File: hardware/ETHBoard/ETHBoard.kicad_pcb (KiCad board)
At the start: 2 copper layers, 25.1 x 12.2 mm, 24 parts, among them J1 Conn_02x04_Odd_Even, J2 Conn_01x02_Pin, U1 LAN8651B1-E_LMX, Y1 X322525MOB4SI

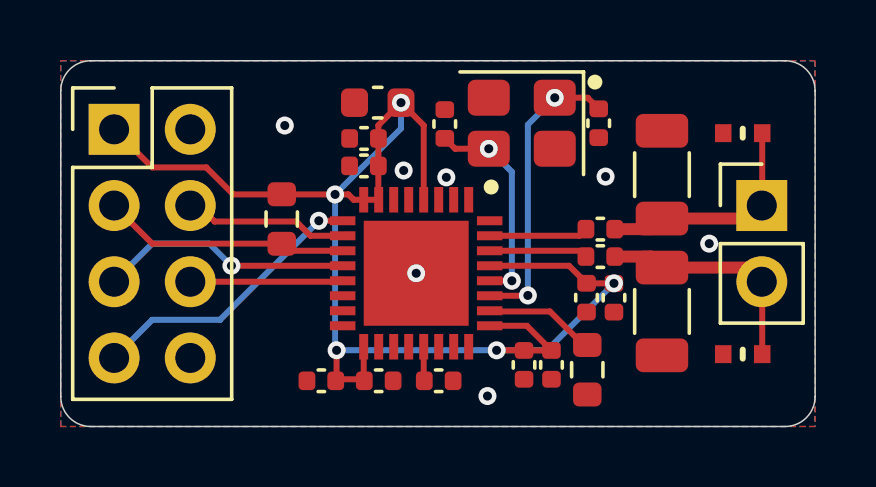
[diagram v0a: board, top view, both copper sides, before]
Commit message: Fixed vias in small pads.
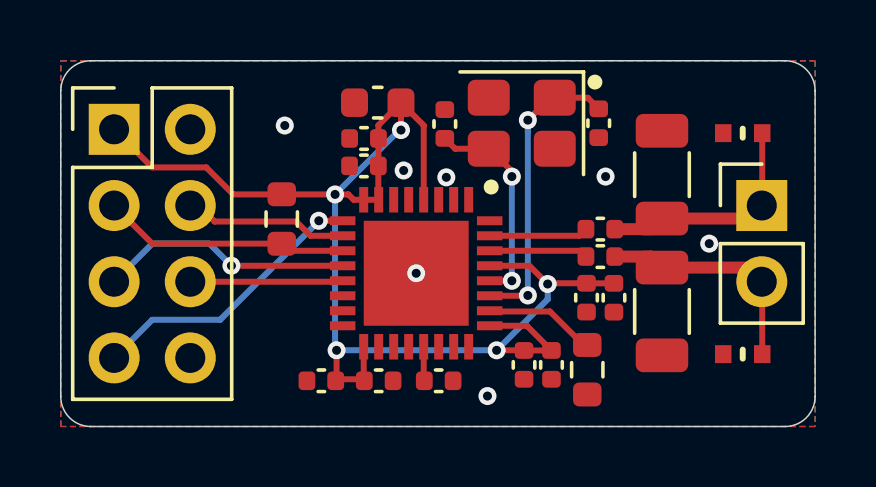
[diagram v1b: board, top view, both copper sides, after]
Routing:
- net 3V3: track 47.8 -> 46.0 mm
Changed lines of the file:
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@@
 		(sheetname "/")
 		(sheetfile "ETHBoard.kicad_sch")
+		(clearance 0.15)
 		(attr smd)
 		(fp_circle
@@
 			(layer "F.Fab")
 		)
-		(fp_text user "${REFERENCE}"
-			(at 0 0 90)
-			(layer "F.Fab")
-			(effects
-				(font
-					(size 1.27 1.27)
-					(thickness 0.254)
-				)
-			)
-		)
 		(pad "1" smd rect
 			(at -2.45 -1.75)
@@
 	)
 	(via
-		(at 85.508 57.884)
+		(at 85.09 54.4576)
 		(size 0.6)
 		(drill 0.3)
 		(layers "F.Cu" "B.Cu")
+		(free yes)
 		(net 2)
 	)
 	(via
-		(at 85.09 54.4576)
+		(at 85.508 57.884)
 		(size 0.6)
 		(drill 0.3)
 		(layers "F.Cu" "B.Cu")
-		(free yes)
 		(net 2)
 	)
@@
 	)
 	(segment
+		(start 89.229843 52.779562)
+		(end 89.976605 52.0328)
+		(width 0.2)
+		(layer "F.Cu")
+		(net 3)
+	)
+	(segment
 		(start 89.2194 58.634)
 		(end 89.2302 58.6232)
@@
 	)
 	(segment
+		(start 89.976605 52.0328)
+		(end 90.127 52.0328)
+		(width 0.2)
+		(layer "F.Cu")
+		(net 3)
+	)
+	(segment
 		(start 87.958 58.634)
 		(end 89.2194 58.634)
@@
 	)
 	(via
-		(at 90.127 52.0328)
+		(at 89.229843 52.779562)
 		(size 0.6)
 		(drill 0.3)
@@
 	)
 	(segment
-		(start 89.2302 52.9296)
-		(end 90.127 52.0328)
+		(start 89.229843 53.16557)
+		(end 89.2302 53.165927)
 		(width 0.2)
 		(layer "B.Cu")
@@
 	)
 	(segment
-		(start 89.2302 58.6232)
-		(end 89.2302 52.9296)
+		(start 89.229843 52.779562)
+		(end 89.229843 53.16557)
 		(width 0.2)
 		(layer "B.Cu")
@@
 	)
 	(segment
+		(start 89.2302 53.165927)
+		(end 89.2302 58.6232)
+		(width 0.2)
+		(layer "B.Cu")
+		(net 3)
+	)
+	(segment
+		(start 87.9466 53.7328)
+		(end 87.927 53.7328)
+		(width 0.2)
+		(layer "F.Cu")
+		(net 4)
+	)
+	(segment
+		(start 88.6968 54.483)
+		(end 87.9466 53.7328)
+		(width 0.2)
+		(layer "F.Cu")
+		(net 4)
+	)
+	(segment
 		(start 86.8062 53.7328)
 		(end 86.4616 53.3882)
@@
 	)
 	(segment
+		(start 88.6968 54.6608)
+		(end 88.6968 54.483)
+		(width 0.2)
+		(layer "F.Cu")
+		(net 4)
+	)
+	(segment
 		(start 88.69669 58.134)
 		(end 87.958 58.134)
@@
 	)
 	(via
-		(at 87.927 53.7328)
+		(at 88.69669 58.134)
 		(size 0.6)
 		(drill 0.3)
@@
 	)
 	(via
-		(at 88.69669 58.134)
+		(at 88.6968 54.6608)
 		(size 0.6)
 		(drill 0.3)
@@
 	)
 	(segment
-		(start 87.927 53.7328)
-		(end 88.69669 54.50249)
+		(start 88.6968 58.13389)
+		(end 88.69669 58.134)
 		(width 0.2)
 		(layer "B.Cu")
@@
 	)
 	(segment
-		(start 88.69669 54.50249)
-		(end 88.69669 58.134)
+		(start 88.6968 54.6608)
+		(end 88.6968 58.13389)
 		(width 0.2)
 		(layer "B.Cu")
@@
 	)
 	(segment
-		(start 91.186 58.2168)
-		(end 90.6032 57.634)
-		(width 0.2)
-		(layer "F.Cu")
-		(net 5)
-	)
-	(segment
 		(start 75.438 53.086)
 		(end 76.708 54.356)
@@
 	)
 	(segment
-		(start 90.6032 57.634)
-		(end 87.958 57.634)
+		(start 85.0014 53.1114)
+		(end 85.0014 52.197)
 		(width 0.2)
 		(layer "F.Cu")
@@
 	)
 	(segment
+		(start 89.8906 58.2422)
+		(end 89.916 58.2168)
+		(width 0.2)
+		(layer "F.Cu")
+		(net 5)
+	)
+	(segment
 		(start 88.1888 60.452)
 		(end 89.098 60.452)
@@
 	)
 	(segment
+		(start 89.2824 57.634)
+		(end 87.958 57.634)
+		(width 0.2)
+		(layer "F.Cu")
+		(net 5)
+	)
+	(segment
 		(start 87.958 59.634)
 		(end 89.1944 59.634)
@@
 	)
 	(segment
+		(start 89.916 58.2168)
+		(end 91.186 58.2168)
+		(width 0.2)
+		(layer "F.Cu")
+		(net 5)
+	)
+	(segment
 		(start 83.2468 55.256)
 		(end 83.4248 55.434)
@@
 	)
 	(segment
+		(start 89.8906 58.2422)
+		(end 89.2824 57.634)
+		(width 0.2)
+		(layer "F.Cu")
+		(net 5)
+	)
+	(segment
 		(start 83.758 55.434)
 		(end 84.258 55.434)
@@
 	)
 	(via
-		(at 82.8548 60.452)
+		(at 89.8906 58.2422)
 		(size 0.6)
 		(drill 0.3)
@@
 	)
 	(via
-		(at 92.1004 58.2194)
+		(at 85.0014 53.1114)
 		(size 0.6)
 		(drill 0.3)
@@
 	)
 	(via
-		(at 85.0014 52.197)
+		(at 82.8548 60.452)
 		(size 0.6)
 		(drill 0.3)
@@
 	)
 	(segment
-		(start 85.0014 53.0586)
-		(end 85.0014 52.197)
+		(start 89.8906 58.2422)
+		(end 89.8906 58.7502)
 		(width 0.2)
 		(layer "B.Cu")
@@
 	)
 	(segment
-		(start 82.8548 60.452)
-		(end 88.1888 60.452)
+		(start 84.9486 53.1114)
+		(end 82.804 55.256)
 		(width 0.2)
 		(layer "B.Cu")
@@
 	)
 	(segment
-		(start 82.804 60.4012)
-		(end 82.804 55.256)
+		(start 82.8548 60.452)
+		(end 88.1888 60.452)
 		(width 0.2)
 		(layer "B.Cu")
@@
 	)
 	(segment
-		(start 82.804 55.256)
-		(end 85.0014 53.0586)
+		(start 89.8906 58.7502)
+		(end 88.1888 60.452)
 		(width 0.2)
 		(layer "B.Cu")
@@
 	)
 	(segment
-		(start 82.8548 60.452)
-		(end 82.804 60.4012)
+		(start 82.804 60.4012)
+		(end 82.804 55.256)
 		(width 0.2)
 		(layer "B.Cu")
@@
 	)
 	(segment
-		(start 89.8678 60.452)
-		(end 92.1004 58.2194)
+		(start 82.8548 60.452)
+		(end 82.804 60.4012)
 		(width 0.2)
 		(layer "B.Cu")
@@
 	)
 	(segment
-		(start 88.1888 60.452)
-		(end 89.8678 60.452)
+		(start 85.0014 53.1114)
+		(end 84.9486 53.1114)
 		(width 0.2)
 		(layer "B.Cu")

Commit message: Rework ETHBoard.
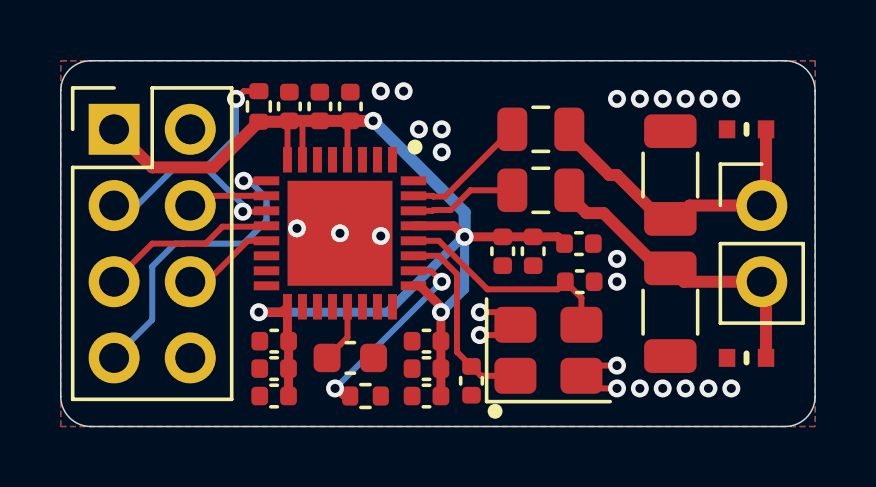
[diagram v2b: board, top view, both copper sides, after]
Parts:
- added C12: 10uF, Capacitor_SMD:C_0402_1005Metric, F.Cu at (80.8, 62.0)
- added C15: 10uF, Capacitor_SMD:C_0402_1005Metric, F.Cu at (85.9, 62.0)
- added C6: 10uF, Capacitor_SMD:C_0402_1005Metric, F.Cu at (90.9, 56.9)
- C1: footprint Capacitor_SMD:C_0402_1005Metric -> Capacitor_SMD:C_0603_1608Metric
- C16: renamed from C13; footprint Capacitor_SMD:C_0402_1005Metric -> Capacitor_SMD:C_0805_2012Metric
- C17: renamed from C14; footprint Capacitor_SMD:C_0402_1005Metric -> Capacitor_SMD:C_0805_2012Metric
- C9: renamed from C4; footprint Capacitor_SMD:C_0603_1608Metric -> Capacitor_SMD:C_0402_1005Metric
- R1, R2: footprint Resistor_SMD:R_0603_1608Metric -> Resistor_SMD:R_0402_1005Metric
- moved C8 12.6 mm to (81.3, 52.3), turned to 90 degrees
- moved C7 10.9 mm to (82.3, 52.3), turned to 90 degrees
- moved C2 9.58 mm to (87.4, 61.5)
- moved Y1 7.62 mm to (89.9, 60.5), turned to 0 degrees
- moved R1 7.45 mm to (83.8, 62.0), turned to 0 degrees
- moved C3 6.92 mm to (91.0, 58.2), turned to 0 degrees
- moved C5 6.78 mm to (89.4, 57.1), turned to -90 degrees
- moved C4 5.43 mm to (88.4, 57.1), turned to -90 degrees
- moved C14 4.17 mm to (85.9, 61.1), turned to 180 degrees
- moved C16 3.87 mm to (89.7, 53.1)
- moved R2 3.83 mm to (80.3, 52.3), turned to -90 degrees
- moved C10 3.73 mm to (80.8, 60.1), turned to 180 degrees
- moved C13 3.35 mm to (85.9, 60.1), turned to 180 degrees
- moved C1 3.04 mm to (83.3, 60.7)
- moved C17 2.97 mm to (89.7, 55.1)
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- renumbered C12 to C10, C10 to C13, C9 to C14, C8 to C4, C7 to C5, C6 to C7, C5 to C8
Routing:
- net GND: track 0.00 -> 5.38 mm, vias 7 -> 25
- net Net-(U1-XTI): track 9.95 -> 6.57 mm, vias 2 -> 0
- net Net-(U1-RBIAS): track 3.73 -> 6.73 mm, vias 0 -> 2
- net /T1S_d-: track 7.65 -> 10.6 mm
- net MISO: track 5.50 -> 2.67 mm
- net SCLK: track 8.45 -> 5.85 mm, vias 1 -> 0
- net /T1S_d+: track 7.67 -> 10.1 mm
- net 3V3: track 46.0 -> 43.6 mm, vias 5 -> 4
- net MOSI: track 5.09 -> 3.10 mm
- net CS_N: track 8.24 -> 9.94 mm, vias 0 -> 2
- net IRQ_N: track 9.52 -> 10.5 mm
- net TRXN: track 3.30 -> 4.23 mm
- net Net-(U1-CCOMP): track 1.08 -> 1.99 mm
- net Net-(U1-XTO): track 7.08 -> 7.50 mm, vias 2 -> 0

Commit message: Added common mode choke.
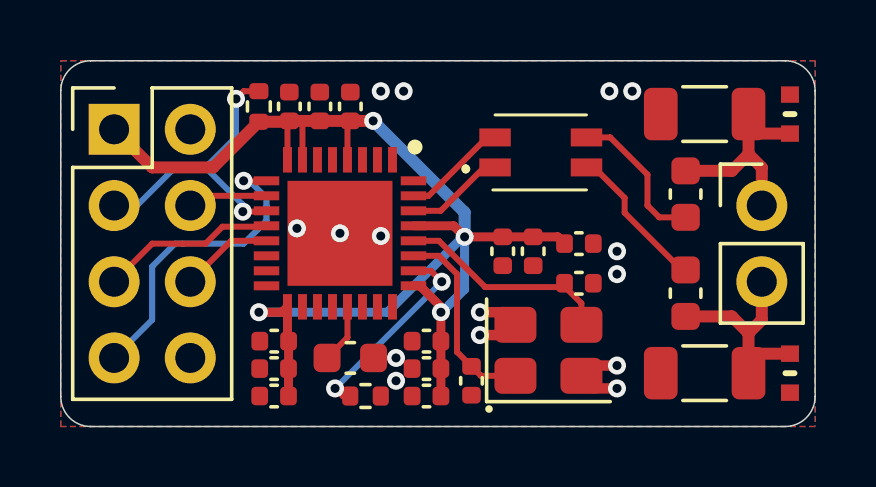
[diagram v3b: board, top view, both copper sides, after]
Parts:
- added FL1: DLW32MH201XK2L, LIB_DLW32MH201XK2L:DLW32MH101XK2L, F.Cu at (89.7, 53.9)
- C16, C17: footprint Capacitor_SMD:C_0805_2012Metric -> Capacitor_SMD:C_0603_1608Metric
- moved C17 5.92 mm to (94.5, 58.5), turned to -90 degrees
- moved C16 5.29 mm to (94.5, 55.2), turned to 90 degrees
- moved R5 2.33 mm to (95.1, 61.2), turned to 180 degrees
- moved R6 2.33 mm to (95.1, 52.6), turned to 0 degrees
- moved RV1 1.53 mm to (98.0, 61.2), turned to -90 degrees
- moved RV2 1.53 mm to (98.0, 52.6), turned to 90 degrees
- moved C3 0.06 mm to (90.9, 58.2)
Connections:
- C16 pad 1: TRXN -> Net-(C16-Pad1)
- C17 pad 1: TRXP -> Net-(C17-Pad1)
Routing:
- net Net-(C16-Pad1): track 0.00 -> 5.01 mm
- net Net-(C17-Pad1): track 0.00 -> 5.01 mm
- net /T1S_d-: track 10.6 -> 7.59 mm
- net /T1S_d+: track 10.1 -> 7.75 mm
- net TRXN: track 4.23 -> 3.52 mm
- net GND: vias 25 -> 15

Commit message: Corrected footprints of varistors.
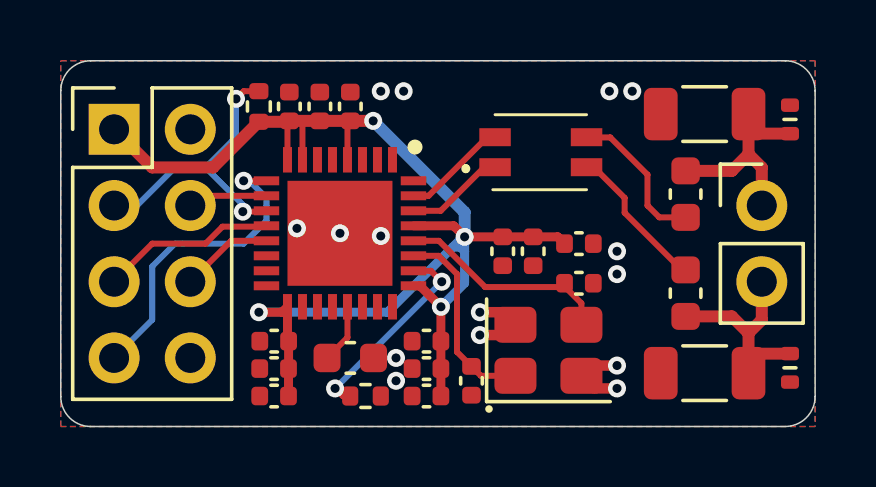
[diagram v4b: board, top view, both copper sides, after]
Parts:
- moved RV1 0.18 mm to (98.0, 61.0)
- moved RV2 0.18 mm to (98.0, 52.8)
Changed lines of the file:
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@@
 	(footprint "LIB_AVRH10C221KT1R5YA8:RESC1005X55N"
 		(layer "F.Cu")
-		(at 97.9678 61.214 -90)
+		(at 97.9678 61.0362 -90)
 		(descr "MMZ1005")
 		(tags "Varistor")
@@
 			)
 		)
+		(property "LCSC" "C2157827"
+			(at 0 0 0)
+			(layer "F.SilkS")
+			(hide yes)
+			(effects
+				(font
+					(size 1.27 1.27)
+					(thickness 0.15)
+				)
+			)
+		)
 		(sheetname "/")
 		(sheetfile "ETHBoard.kicad_sch")
 		(attr smd)
 		(fp_line
-			(start 0 -0.15)
-			(end 0 0.15)
+			(start 0 -0.2)
+			(end 0 0.2)
 			(stroke
-				(width 0.2)
+				(width 0.12)
 				(type solid)
 			)
@@
 		)
 		(fp_line
-			(start -1.175 0.55)
-			(end -1.175 -0.55)
+			(start -0.95 0.55)
+			(end -0.95 -0.55)
 			(stroke
 				(width 0.05)
@@
 		)
 		(fp_line
-			(start 1.175 0.55)
-			(end -1.175 0.55)
+			(start 0.95 0.55)
+			(end -0.95 0.55)
 			(stroke
 				(width 0.05)
@@
 		)
 		(fp_line
-			(start -1.175 -0.55)
-			(end 1.175 -0.55)
+			(start -0.95 -0.55)
+			(end 0.95 -0.55)
 			(stroke
 				(width 0.05)
@@
 		)
 		(fp_line
-			(start 1.175 -0.55)
-			(end 1.175 0.55)
+			(start 0.95 -0.55)
+			(end 0.95 0.55)
 			(stroke
 				(width 0.05)
@@
 			(layer "F.Fab")
 		)
-		(pad "1" smd rect
-			(at -0.65 0 270)
-			(size 0.55 0.6)
+		(pad "1" smd roundrect
+			(at -0.475 0 270)
+			(size 0.45 0.6)
 			(layers "F.Cu" "F.Mask" "F.Paste")
+			(roundrect_rratio 0.25)
 			(net 7 "/T1S_d+")
 			(pinfunction "1")
 			(pintype "passive")
 		)
-		(pad "2" smd rect
-			(at 0.65 0 270)
-			(size 0.55 0.6)
+		(pad "2" smd roundrect
+			(at 0.475 0 270)
+			(size 0.45 0.6)
 			(layers "F.Cu" "F.Mask" "F.Paste")
+			(roundrect_rratio 0.25)
 			(net 2 "GND")
 			(pinfunction "2")
@@
 	(footprint "LIB_AVRH10C221KT1R5YA8:RESC1005X55N"
 		(layer "F.Cu")
-		(at 97.9678 52.578 90)
+		(at 97.9678 52.7558 90)
 		(descr "MMZ1005")
 		(tags "Varistor")
@@
 			)
 		)
+		(property "LCSC" "C2157827"
+			(at 0 0 0)
+			(layer "F.SilkS")
+			(hide yes)
+			(effects
+				(font
+					(size 1.27 1.27)
+					(thickness 0.15)
+				)
+			)
+		)
 		(sheetname "/")
 		(sheetfile "ETHBoard.kicad_sch")
 		(attr smd)
 		(fp_line
-			(start 0 -0.15)
-			(end 0 0.15)
+			(start 0 -0.2)
+			(end 0 0.2)
 			(stroke
-				(width 0.2)
+				(width 0.12)
 				(type solid)
 			)
@@
 		)
 		(fp_line
-			(start 1.175 -0.55)
-			(end 1.175 0.55)
+			(start 0.95 -0.55)
+			(end 0.95 0.55)
 			(stroke
 				(width 0.05)
@@
 		)
 		(fp_line
-			(start -1.175 -0.55)
-			(end 1.175 -0.55)
+			(start -0.95 -0.55)
+			(end 0.95 -0.55)
 			(stroke
 				(width 0.05)
@@
 		)
 		(fp_line
-			(start 1.175 0.55)
-			(end -1.175 0.55)
+			(start 0.95 0.55)
+			(end -0.95 0.55)
 			(stroke
 				(width 0.05)
@@
 		)
 		(fp_line
-			(start -1.175 0.55)
-			(end -1.175 -0.55)
+			(start -0.95 0.55)
+			(end -0.95 -0.55)
 			(stroke
 				(width 0.05)
@@
 			(layer "F.Fab")
 		)
-		(pad "1" smd rect
-			(at -0.65 0 90)
-			(size 0.55 0.6)
+		(pad "1" smd roundrect
+			(at -0.475 0 90)
+			(size 0.45 0.6)
 			(layers "F.Cu" "F.Mask" "F.Paste")
+			(roundrect_rratio 0.25)
 			(net 6 "/T1S_d-")
 			(pinfunction "1")
 			(pintype "passive")
 		)
-		(pad "2" smd rect
-			(at 0.65 0 90)
-			(size 0.55 0.6)
+		(pad "2" smd roundrect
+			(at 0.475 0 90)
+			(size 0.45 0.6)
 			(layers "F.Cu" "F.Mask" "F.Paste")
+			(roundrect_rratio 0.25)
 			(net 2 "GND")
 			(pinfunction "2")
@@
 	(footprint "LIB_DLW32MH201XK2L:DLW32MH101XK2L"
 		(layer "F.Cu")
-		(at 89.661 53.856 180)
+		(at 89.662 53.848 180)
 		(descr "DLW32MH_XK2 L=3.2 W=2.5 T=2.5")
 		(tags "Filter")
@@
 		(attr smd)
 		(fp_line
-			(start 2.5 -0.5)
-			(end 2.5 -0.5)
-			(stroke
-				(width 0.2)
-				(type solid)
-			)
-			(layer "F.SilkS")
-		)
-		(fp_line
-			(start 2.5 -0.6)
-			(end 2.5 -0.6)
-			(stroke
-				(width 0.2)
-				(type solid)
-			)
-			(layer "F.SilkS")
-		)
-		(fp_line
 			(start 1.6 -1.25)
 			(end -1.525 -1.25)
@@
 			(layer "F.SilkS")
 		)
-		(fp_line
-			(start 3.55 2.25)
-			(end 3.55 -2.25)
-			(stroke
-				(width 0.1)
-				(type solid)
-			)
-			(layer "F.CrtYd")
-		)
-		(fp_line
-			(start 3.55 -2.25)
-			(end -3.05 -2.25)
-			(stroke
-				(width 0.1)
-				(type solid)
-			)
-			(layer "F.CrtYd")
-		)
-		(fp_line
-			(start -3.05 2.25)
-			(end 3.55 2.25)
-			(stroke
-				(width 0.1)
-				(type solid)
-			)
-			(layer "F.CrtYd")
-		)
-		(fp_line
+		(fp_rect
 			(start -3.05 -2.25)
-			(end -3.05 2.25)
+			(end 3.55 2.25)
 			(stroke
 				(width 0.1)
 				(type solid)
 			)
+			(fill no)
 			(layer "F.CrtYd")
 		)
-		(fp_line
-			(start 1.6 1.25)
-			(end 1.6 -1.25)
-			(stroke
-				(width 0.2)
-				(type solid)
-			)
-			(layer "F.Fab")
-		)
-		(fp_line
-			(start 1.6 -1.25)
-			(end -1.6 -1.25)
-			(stroke
-				(width 0.2)
-				(type solid)
-			)
-			(layer "F.Fab")
-		)
-		(fp_line
-			(start -1.6 1.25)
-			(end 1.6 1.25)
-			(stroke
-				(width 0.2)
-				(type solid)
-			)
-			(layer "F.Fab")
-		)
-		(fp_line
+		(fp_rect
 			(start -1.6 -1.25)
-			(end -1.6 1.25)
+			(end 1.6 1.25)
 			(stroke
 				(width 0.2)
 				(type solid)
 			)
+			(fill no)
 			(layer "F.Fab")
 		)
@@
 		(model "DLW32MH201XK2L.step"
 			(offset
-				(xyz -0.1199999955 -0.05999999776 0)
+				(xyz 0 0 0)
 			)
 			(scale
@@
 	)
 	(segment
+		(start 86.332 59.0016)
+		(end 86.332 60.1472)
+		(width 0.3)
+		(layer "F.Cu")
+		(net 5)
+	)
+	(segment
 		(start 81.25 52.834)
 		(end 81.28 52.804)
@@
 	)
 	(segment
+		(start 85.6324 58.302)
+		(end 85.418 58.302)
+		(width 0.3)
+		(layer "F.Cu")
+		(net 5)
+	)
+	(segment
 		(start 76.708 54.356)
 		(end 78.74 54.356)
@@
 	)
 	(segment
-		(start 86.332 59.0016)
-		(end 85.6324 58.302)
-		(width 0.3)
-		(layer "F.Cu")
-		(net 5)
-	)
-	(segment
 		(start 84.074 52.804)
 		(end 83.312 52.804)
@@
 	)
 	(segment
-		(start 86.332 59.182)
-		(end 86.332 59.0016)
-		(width 0.3)
-		(layer "F.Cu")
-		(net 5)
-	)
-	(segment
 		(start 81.218 54.102)
 		(end 81.218 52.866)
@@
 	)
 	(segment
-		(start 86.332 59.182)
-		(end 86.332 60.1472)
-		(width 0.3)
-		(layer "F.Cu")
-		(net 5)
-	)
-	(segment
 		(start 90.226 56.67)
 		(end 90.452 56.896)
@@
 	)
 	(segment
-		(start 85.6324 58.302)
-		(end 85.418 58.302)
-		(width 0.3)
+		(start 83.218 54.102)
+		(end 83.218 52.898)
+		(width 0.2)
 		(layer "F.Cu")
 		(net 5)
 	)
 	(segment
-		(start 83.218 54.102)
-		(end 83.218 52.898)
-		(width 0.2)
+		(start 86.332 59.0016)
+		(end 85.6324 58.302)
+		(width 0.3)
 		(layer "F.Cu")
 		(net 5)
@@
 	)
 	(via
-		(at 86.332 59.182)
+		(at 86.332 59.0016)
 		(size 0.6)
 		(drill 0.3)
@@
 	)
 	(segment
-		(start 87.122 56.67)
-		(end 87.122 58.42)
+		(start 86.9823 57.0103)
+		(end 87.122 57.15)
 		(width 0.3)
 		(layer "B.Cu")
@@
 	)
 	(segment
-		(start 87.122 56.67)
-		(end 87.0686 56.67)
+		(start 86.332 59.0016)
+		(end 87.122 58.2116)
+		(width 0.3)
+		(layer "B.Cu")
+		(net 5)
+	)
+	(segment
+		(start 86.7283 57.0103)
+		(end 86.9823 57.0103)
+		(width 0.3)
+		(layer "B.Cu")
+		(net 5)
+	)
+	(segment
+		(start 87.122 58.2116)
+		(end 87.122 57.15)
 		(width 0.3)
 		(layer "B.Cu")
@@
 	)
 	(segment
-		(start 86.36 59.182)
-		(end 86.332 59.182)
+		(start 87.122 56.67)
+		(end 87.0686 56.67)
 		(width 0.3)
 		(layer "B.Cu")
@@
 	)
 	(segment
+		(start 86.7283 57.0103)
+		(end 84.5566 59.182)
+		(width 0.3)
+		(layer "B.Cu")
+		(net 5)
+	)
+	(segment
 		(start 84.074 52.804)
 		(end 87.122 55.852)
@@
 	(segment
 		(start 87.0686 56.67)
-		(end 84.5566 59.182)
+		(end 86.7283 57.0103)
 		(width 0.3)
 		(layer "B.Cu")
@@
 	)
 	(segment
-		(start 87.122 58.42)
-		(end 86.36 59.182)
+		(start 87.122 57.15)
+		(end 87.122 56.67)
 		(width 0.3)
 		(layer "B.Cu")
@@
 		(polygon
 			(pts
-				(xy 93.897759 55.791404) (xy 92.018159 53.886404) (xy 92.018159 56.350204) (xy 93.897759 58.255204)
+				(xy 93.897759 57.51602) (xy 92.018159 55.61102) (xy 92.018159 56.53) (xy 93.897759 58.45582)
 			)
 		)
@@
 		(polygon
 			(pts
-				(xy 93.5228 51.816) (xy 98.806 51.816) (xy 98.806 61.976) (xy 93.5228 61.976)
+				(xy 93.5228 51.816) (xy 97.028 51.816) (xy 97.028 52.324) (xy 98.806 52.324) (xy 98.806 61.468)
+				(xy 97.028 61.468) (xy 97.028 61.976) (xy 93.5228 61.976)
 			)
 		)
